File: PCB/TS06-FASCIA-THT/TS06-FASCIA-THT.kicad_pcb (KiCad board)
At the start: 2 copper layers, 176 x 52 mm, 18 parts, among them J1 PH 6 THT, SW1 SR25 6-pos, SW2 FIELD, SW3 SUB, SW4 MINUS, SW5 PLUS

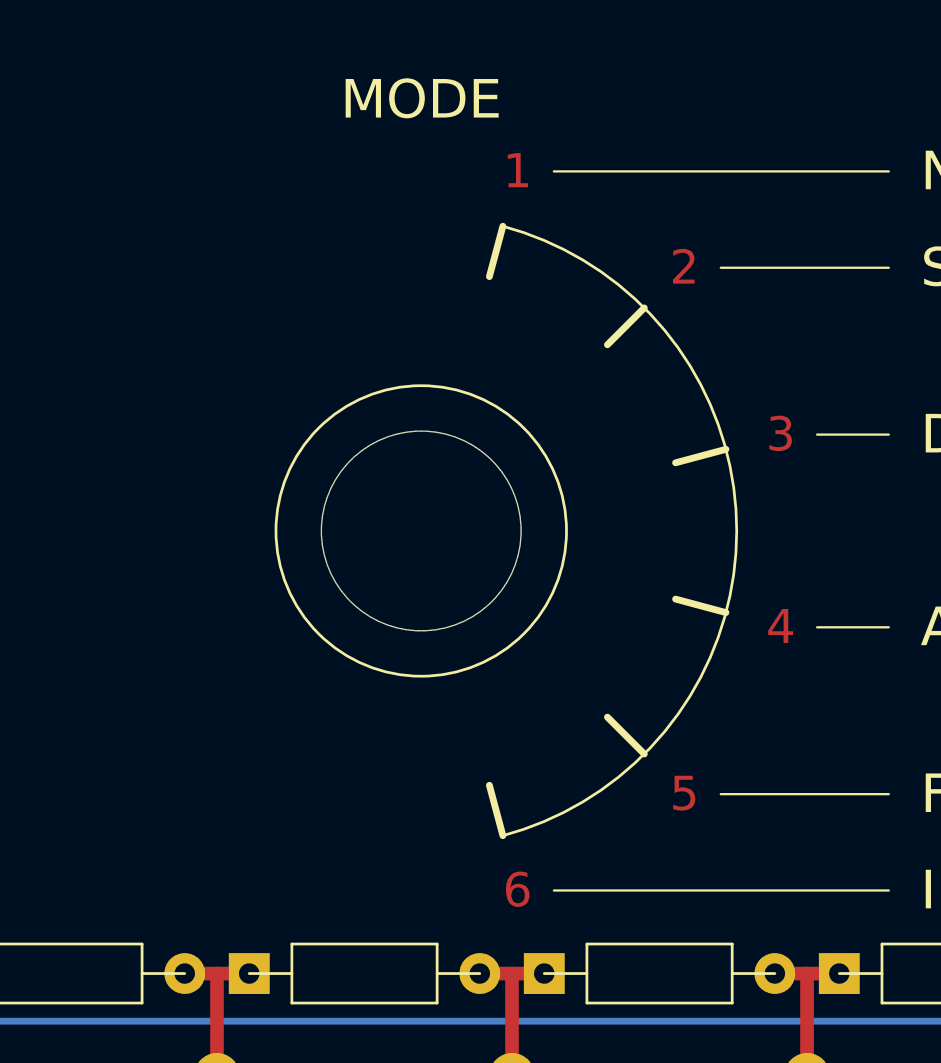
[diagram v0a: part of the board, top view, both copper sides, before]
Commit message: PCB: TS06-FASCIA-THT cosmetic rework and GND pour fill
Cosmetic trace tidy-up around the 6-pin connector done by hand in
KiCad, and the GND pour re-filled over the reworked layout. Checked
clean: 18 footprints/46 pads, 34 tracks/0 vias, schematic and board
agree on all 12 nets, pour reaches all 7 GND pads.

Co-Authored-By: Claude Sonnet 5 <noreply@anthropic.com>
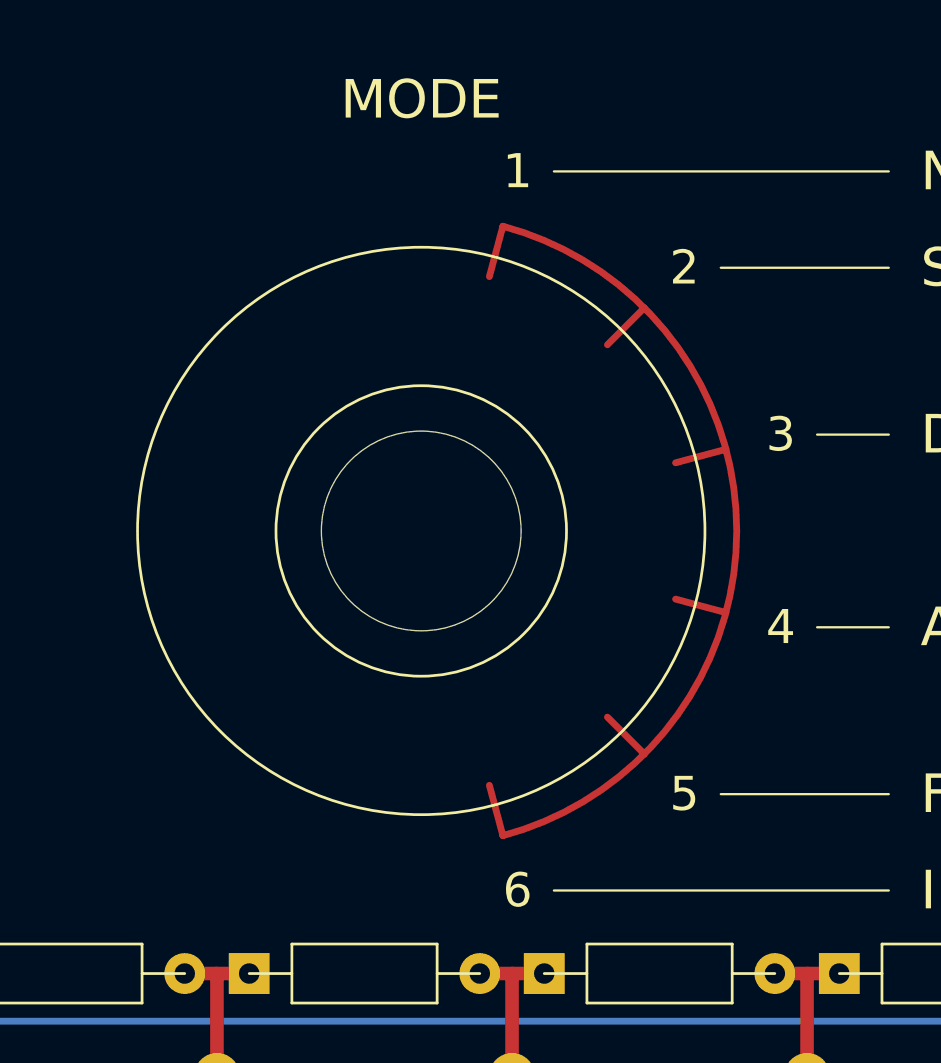
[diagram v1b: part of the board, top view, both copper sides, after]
